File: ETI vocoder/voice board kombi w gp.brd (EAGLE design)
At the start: 160 x 60.3 mm, 170 parts, among them IC1 TL072P, IC1. TL072P, IC2 TL072P, IC2. TL072P, IC3 TL081P, IC3. TL081P, IC4 TL081P, IC4. TL081P, IC5 TL072P, IC6 LM13600AN, IC7 TL072P, IC7. TL072P, P1. C-OR-R050_075-030X100, P10. C-OR-R050_075-030X100, P13. C-OR-R050_075-030X100, P14. C-OR-R050_075-030X100, P16 C-OR-R050_075-030X100, P2. C-OR-R050_075-030X100, P5. C-OR-R050_075-030X100, P6. C-OR-R050_075-030X100, P8 C-OR-R050_075-030X100, P9. C-OR-R050_075-030X100, Q1 BF244C, Q1. BF244C, Q2 BC212L, Q2. BC212L

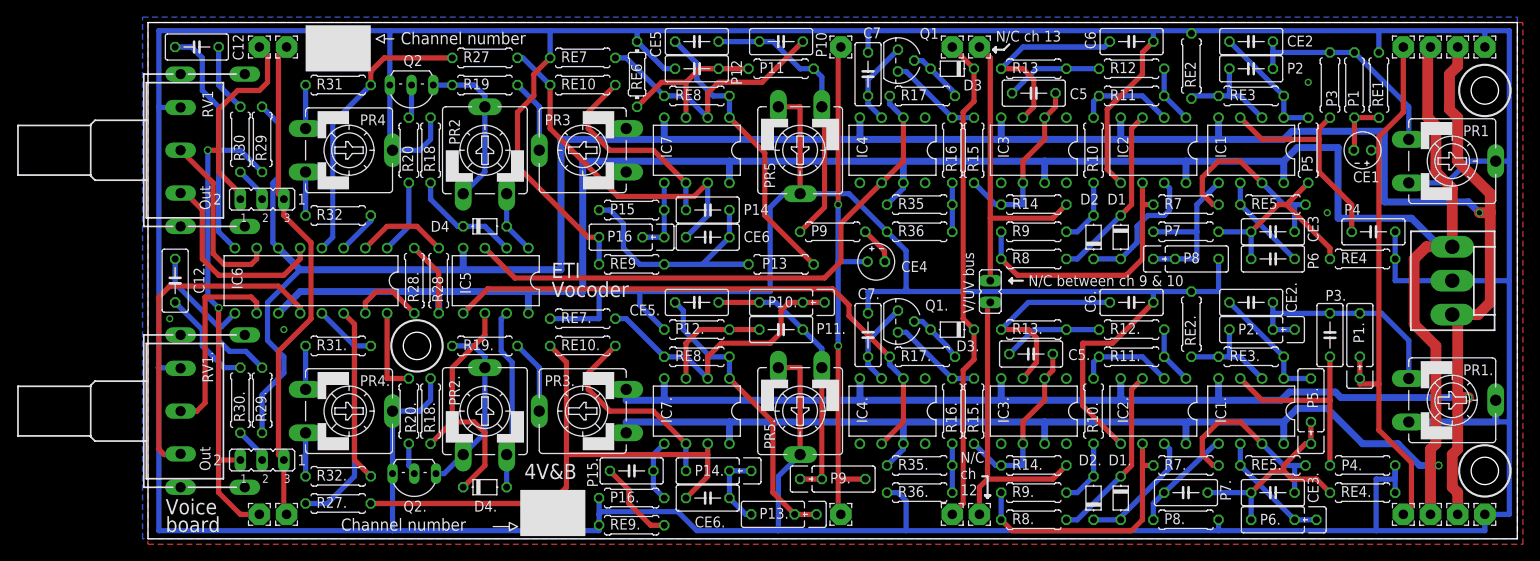
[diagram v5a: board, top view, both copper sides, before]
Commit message: Reduced board width to 2.355 inch (59.82 mm), this gives a spacing between boards of 1.1 mm, allowing a slight inaccuracy when mounting the cards next to each other
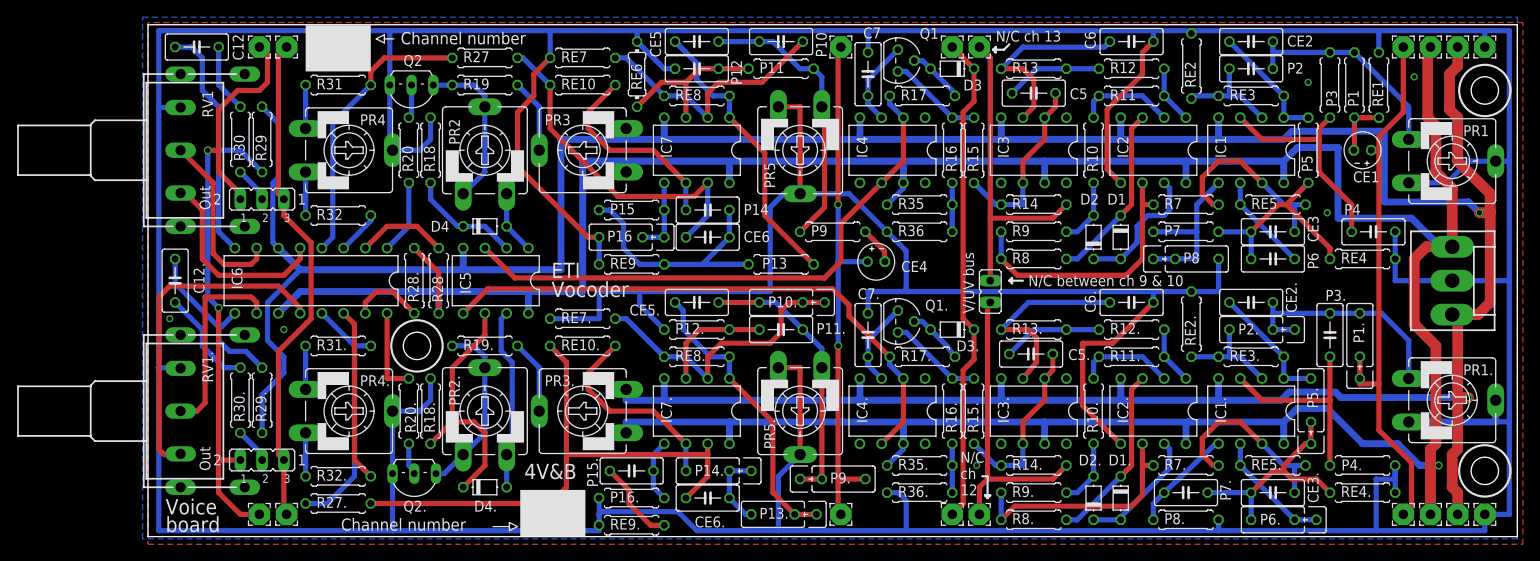
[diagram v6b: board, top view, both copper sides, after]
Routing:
- net N$54: track 30.9 -> 28.2 mm
- net GND: vias 4 -> 6
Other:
- board size 160 x 60.3 mm -> 160 x 59.8 mm
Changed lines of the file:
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@@
 <setting verticaltext="up"/>
 </settings>
-<grid distance="0.0125" unitdist="inch" unit="inch" style="dots" multiple="1" display="yes" altdistance="0.025" altunitdist="inch" altunit="inch"/>
+<grid distance="0.0125" unitdist="inch" unit="mil" style="dots" multiple="1" display="yes" altdistance="0.025" altunitdist="inch" altunit="inch"/>
 <layers>
 <layer number="1" name="Top" color="4" fill="1" visible="yes" active="yes"/>
@@
 <board>
 <plain>
-<wire x1="0" y1="0" x2="160" y2="0" width="0" layer="20"/>
-<wire x1="160" y1="0" x2="160" y2="60.325" width="0" layer="20"/>
-<wire x1="160" y1="60.325" x2="0" y2="60.325" width="0" layer="20"/>
-<wire x1="0" y1="60.325" x2="0" y2="0" width="0" layer="20"/>
+<wire x1="0" y1="0.254" x2="160" y2="0.254" width="0" layer="20"/>
+<wire x1="160" y1="0.254" x2="160" y2="60.071" width="0" layer="20"/>
+<wire x1="160" y1="60.071" x2="0" y2="60.071" width="0" layer="20"/>
+<wire x1="0" y1="60.071" x2="0" y2="0.254" width="0" layer="20"/>
 <hole x="156.21" y="52.3875" drill="3.2"/>
 <circle x="156.21" y="52.3875" radius="3" width="0.254" layer="25"/>
@@
 <wire x1="52.705" y1="1.905" x2="53.0225" y2="1.5875" width="0.6096" layer="16"/>
 <wire x1="53.0225" y1="1.5875" x2="52.705" y2="1.5875" width="0.6096" layer="16"/>
+<via x="147.955" y="53.975" extent="1-16" drill="0.5"/>
+<via x="96.8375" y="8.5725" extent="1-16" drill="0.5"/>
 </signal>
 <signal name="N$5">
@@
 <wire x1="99.695" y1="5.3975" x2="99.695" y2="2.2225" width="0.6096" layer="16"/>
 <wire x1="116.205" y1="11.1125" x2="116.205" y2="8.5725" width="0.6096" layer="1"/>
-<wire x1="116.205" y1="8.5725" x2="116.205" y2="2.2225" width="0.6096" layer="1"/>
-<wire x1="116.205" y1="2.2225" x2="114.935" y2="0.9525" width="0.6096" layer="1"/>
-<wire x1="114.935" y1="0.9525" x2="100.965" y2="0.9525" width="0.6096" layer="1"/>
-<wire x1="100.965" y1="0.9525" x2="99.695" y2="2.2225" width="0.6096" layer="1"/>
+<wire x1="116.205" y1="8.5725" x2="116.205" y2="5.08" width="0.6096" layer="1"/>
+<wire x1="116.205" y1="5.08" x2="114.935" y2="3.81" width="0.6096" layer="1"/>
+<wire x1="114.935" y1="3.81" x2="101.2825" y2="3.81" width="0.6096" layer="1"/>
+<wire x1="101.2825" y1="3.81" x2="99.695" y2="2.2225" width="0.6096" layer="1"/>
 <wire x1="117.475" y1="8.5725" x2="116.205" y2="8.5725" width="0.6096" layer="1"/>
 </signal>

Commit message: Updated trimpot names and positions
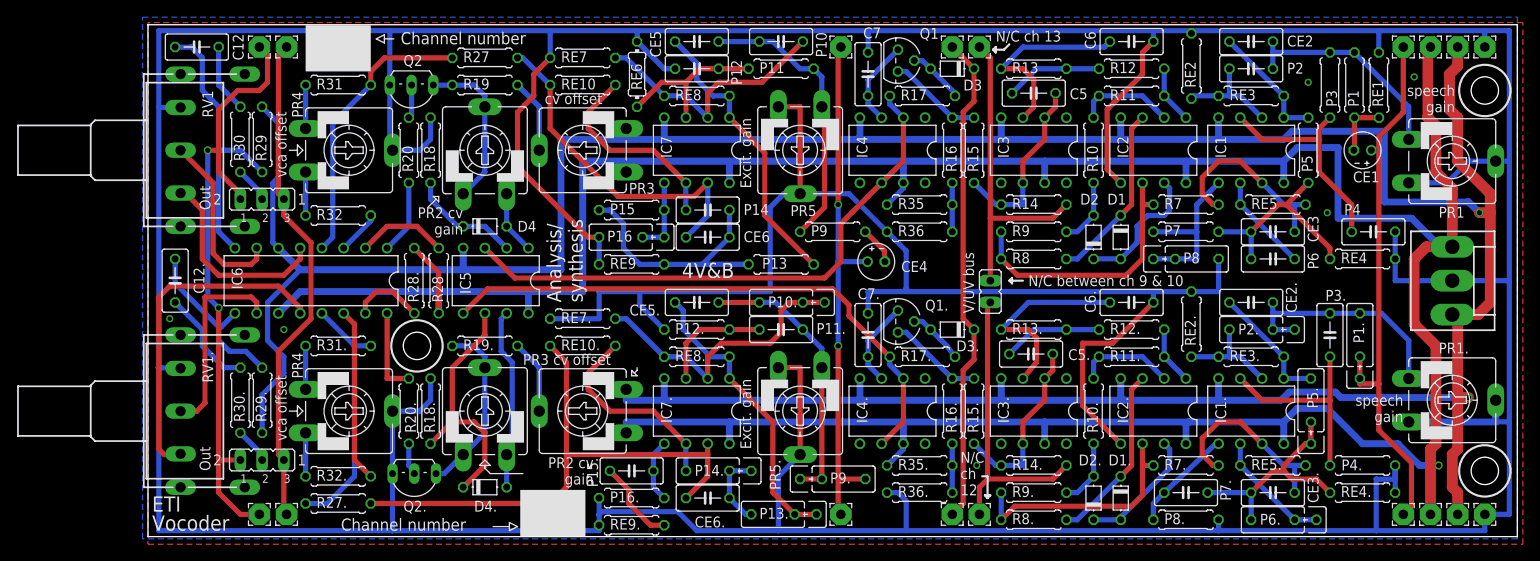
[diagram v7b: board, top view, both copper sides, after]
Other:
- board text added: "Analysis/ synthesis"
- board text added: "Excit. gain"
- board text added: "PR2 cv gain"
- board text added: "PR3"
- board text added: "PR3 cv offset"
- board text added: "PR4"
- board text added: "cv offset"
- board text added: "speech gain"
- board text added: "vca offset"
- board text removed: "Voice"
- board text removed: "board"
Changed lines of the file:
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@@
 <grid distance="0.0125" unitdist="inch" unit="mil" style="dots" multiple="1" display="yes" altdistance="0.025" altunitdist="inch" altunit="inch"/>
 <layers>
-<layer number="1" name="Top" color="4" fill="1" visible="yes" active="yes"/>
+<layer number="1" name="Top" color="4" fill="1" visible="no" active="yes"/>
 <layer number="2" name="Route2" color="1" fill="3" visible="no" active="no"/>
 <layer number="3" name="Route3" color="4" fill="3" visible="no" active="no"/>
@@
 <hole x="156.21" y="7.9375" drill="3.2"/>
 <circle x="156.21" y="7.9375" radius="3" width="0.254" layer="25"/>
-<text x="43.97375" y="6.985" size="1.778" layer="25" font="vector">4V&amp;B</text>
+<text x="62.38875" y="30.48" size="1.778" layer="25" font="vector">4V&amp;B</text>
 <text x="93.6625" y="55.5625" size="1.27" layer="26" font="vector" rot="MR270">Slew</text>
 <text x="98.425" y="55.5625" size="1.27" layer="26" font="vector" rot="MR270">V/UV</text>
@@
 <wire x1="43.18" y1="1.42875" x2="42.2275" y2="0.9525" width="0.15" layer="25"/>
 <wire x1="42.2275" y1="0.9525" x2="42.2275" y2="1.42875" width="0.15" layer="25"/>
-<text x="2.06375" y="2.8575" size="1.778" layer="25">Voice</text>
-<text x="2.06375" y="0.79375" size="1.778" layer="25">board</text>
-<text x="47.14875" y="30.48" size="1.778" layer="25">ETI</text>
-<text x="47.14875" y="28.2575" size="1.778" layer="25">Vocoder</text>
+<text x="0.47625" y="3.175" size="1.778" layer="25">ETI</text>
+<text x="0.47625" y="0.9525" size="1.778" layer="25">Vocoder</text>
 <text x="153.035" y="23.33625" size="1.27" layer="26" rot="MR270">ETI Vocoder</text>
 <text x="153.82875" y="48.10125" size="1.27" layer="26" rot="MR270">Dual voice
 board v1.0</text>
+<text x="50.8" y="27.6225" size="1.6764" layer="25" rot="R90">Analysis/
+synthesis</text>
+<text x="152.7175" y="53.0225" size="1.27" layer="25" rot="R180">speech
+gain</text>
+<text x="146.685" y="16.8275" size="1.27" layer="25" rot="R180">speech
+gain</text>
+<text x="70.485" y="10.4775" size="1.27" layer="25" rot="R90">Excit. gain</text>
+<text x="70.485" y="40.9575" size="1.27" layer="25" rot="R90">Excit. gain</text>
+<text x="46.355" y="50.8" size="1.27" layer="25">cv offset</text>
+<text x="43.815" y="20.32" size="1.27" layer="25">PR3 cv offset</text>
+<text x="52.07" y="9.525" size="1.27" layer="25" rot="R180">PR2 cv
+gain</text>
+<text x="16.1925" y="42.2275" size="1.27" layer="25" rot="R90">vca offset</text>
+<text x="16.1925" y="11.43" size="1.27" layer="25" rot="R90">vca offset</text>
+<wire x1="43.815" y1="7.62" x2="40.005" y2="7.62" width="0.127" layer="25"/>
+<wire x1="40.005" y1="7.62" x2="39.37" y2="8.255" width="0.127" layer="25"/>
+<wire x1="39.37" y1="8.255" x2="39.37" y2="8.5725" width="0.127" layer="25"/>
+<wire x1="39.37" y1="8.5725" x2="38.735" y2="8.5725" width="0.127" layer="25"/>
+<wire x1="38.735" y1="8.5725" x2="39.37" y2="9.2075" width="0.127" layer="25"/>
+<wire x1="39.37" y1="9.2075" x2="40.005" y2="8.5725" width="0.127" layer="25"/>
+<wire x1="40.005" y1="8.5725" x2="39.37" y2="8.5725" width="0.127" layer="25"/>
+<wire x1="57.15" y1="20.0025" x2="57.15" y2="19.685" width="0.127" layer="25"/>
+<wire x1="57.15" y1="19.685" x2="56.8325" y2="19.3675" width="0.127" layer="25"/>
+<wire x1="56.8325" y1="19.3675" x2="56.515" y2="19.685" width="0.127" layer="25"/>
+<wire x1="56.515" y1="19.685" x2="56.515" y2="19.05" width="0.127" layer="25"/>
+<wire x1="56.515" y1="19.05" x2="57.15" y2="19.05" width="0.127" layer="25"/>
+<wire x1="57.15" y1="19.05" x2="56.8325" y2="19.3675" width="0.127" layer="25"/>
+<text x="36.83" y="38.735" size="1.27" layer="25" rot="R180">PR2 cv
+gain</text>
+<wire x1="32.7025" y1="38.735" x2="33.655" y2="39.6875" width="0.127" layer="25"/>
+<wire x1="33.655" y1="39.6875" x2="33.3375" y2="40.005" width="0.127" layer="25"/>
+<wire x1="33.3375" y1="40.005" x2="33.9725" y2="40.005" width="0.127" layer="25"/>
+<wire x1="33.9725" y1="40.005" x2="33.9725" y2="39.37" width="0.127" layer="25"/>
+<wire x1="33.9725" y1="39.37" x2="33.655" y2="39.6875" width="0.127" layer="25"/>
+<wire x1="16.51" y1="45.4025" x2="17.4625" y2="45.4025" width="0.127" layer="25"/>
+<wire x1="17.4625" y1="45.4025" x2="17.4625" y2="46.0375" width="0.127" layer="25"/>
+<wire x1="17.4625" y1="46.0375" x2="18.0975" y2="45.4025" width="0.127" layer="25"/>
+<wire x1="18.0975" y1="45.4025" x2="17.4625" y2="44.7675" width="0.127" layer="25"/>
+<wire x1="17.4625" y1="44.7675" x2="17.4625" y2="45.4025" width="0.127" layer="25"/>
+<text x="18.0975" y="49.2125" size="1.27" layer="25" rot="R90">PR4</text>
+<text x="18.0975" y="18.7325" size="1.27" layer="25" rot="R90">PR4</text>
+<wire x1="16.51" y1="14.9225" x2="17.4625" y2="14.9225" width="0.127" layer="25"/>
+<wire x1="17.4625" y1="14.9225" x2="17.4625" y2="15.5575" width="0.127" layer="25"/>
+<wire x1="17.4625" y1="15.5575" x2="18.0975" y2="14.9225" width="0.127" layer="25"/>
+<wire x1="18.0975" y1="14.9225" x2="17.4625" y2="14.2875" width="0.127" layer="25"/>
+<wire x1="17.4625" y1="14.2875" x2="17.4625" y2="14.9225" width="0.127" layer="25"/>
+<text x="56.1975" y="40.3225" size="1.27" layer="25">PR3</text>
 </plain>
 <attributes>
@@
 </element>
 <element name="PR1" library="pot" package="CA9V" value="" x="152.4" y="44.1325" smashed="yes" rot="R270">
-<attribute name="NAME" x="153.67" y="47.0535" size="1.27" layer="25" ratio="10"/>
+<attribute name="NAME" x="150.8125" y="37.5285" size="1.27" layer="25" ratio="10"/>
 <attribute name="VALUE" x="147.32" y="37.4015" size="1.27" layer="27" ratio="10"/>
 </element>
@@
 </element>
 <element name="D4" library="diode" package="D-5" value="" x="39.37" y="36.5125" smashed="yes">
-<attribute name="NAME" x="33.02" y="35.8775" size="1.27" layer="25" ratio="10"/>
+<attribute name="NAME" x="43.18" y="35.8775" size="1.27" layer="25" ratio="10"/>
 <attribute name="VALUE" x="37.465" y="33.9725" size="1.27" layer="27" ratio="10"/>
 </element>
 <element name="PR2" library="pot" package="CA9V" value="" x="39.37" y="45.4025" smashed="yes">
-<attribute name="NAME" x="36.449" y="46.0375" size="1.27" layer="25" ratio="10" rot="R90"/>
 <attribute name="VALUE" x="46.101" y="40.3225" size="1.27" layer="27" ratio="10" rot="R90"/>
 </element>
@@
 </element>
 <element name="PR3" library="pot" package="CA9V" value="" x="50.8" y="45.4025" smashed="yes" rot="R90">
-<attribute name="NAME" x="46.355" y="48.3235" size="1.27" layer="25" ratio="10"/>
 <attribute name="VALUE" x="55.88" y="52.1335" size="1.27" layer="27" ratio="10" rot="R180"/>
 </element>
@@
 </element>
 <element name="PR4" library="pot" package="CA9V" value="" x="23.495" y="45.4025" smashed="yes" rot="R270">
-<attribute name="NAME" x="24.765" y="48.3235" size="1.27" layer="25" ratio="10"/>
 <attribute name="VALUE" x="18.415" y="38.6715" size="1.27" layer="27" ratio="10"/>
 </element>
 <element name="PR5" library="pot" package="CA9V" value="" x="76.2" y="45.4025" smashed="yes" rot="R180">
-<attribute name="NAME" x="73.279" y="40.9575" size="1.27" layer="25" ratio="10" rot="R90"/>
+<attribute name="NAME" x="78.105" y="38.989" size="1.27" layer="25" ratio="10" rot="R180"/>
 <attribute name="VALUE" x="69.469" y="50.4825" size="1.27" layer="27" ratio="10" rot="R270"/>
 </element>
@@
 </element>
 <element name="PR1." library="pot" package="CA9V" value="" x="152.4" y="16.1925" smashed="yes" rot="R270">
-<attribute name="NAME" x="153.67" y="19.1135" size="1.27" layer="25" ratio="10"/>
+<attribute name="NAME" x="150.8125" y="21.6535" size="1.27" layer="25" ratio="10"/>
 <attribute name="VALUE" x="147.32" y="9.4615" size="1.27" layer="27" ratio="10"/>
 </element>
@@
 </element>
 <element name="PR2." library="pot" package="CA9V" value="" x="39.37" y="14.9225" smashed="yes">
-<attribute name="NAME" x="36.449" y="15.5575" size="1.27" layer="25" ratio="10" rot="R90"/>
 <attribute name="VALUE" x="46.101" y="9.8425" size="1.27" layer="27" ratio="10" rot="R90"/>
 </element>
@@
 </element>
 <element name="PR3." library="pot" package="CA9V" value="" x="50.8" y="14.9225" smashed="yes" rot="R90">
-<attribute name="NAME" x="46.355" y="17.8435" size="1.27" layer="25" ratio="10"/>
 <attribute name="VALUE" x="55.88" y="21.6535" size="1.27" layer="27" ratio="10" rot="R180"/>
 </element>
@@
 </element>
 <element name="PR4." library="pot" package="CA9V" value="" x="23.495" y="14.9225" smashed="yes" rot="R270">
-<attribute name="NAME" x="24.765" y="17.8435" size="1.27" layer="25" ratio="10"/>
 <attribute name="VALUE" x="18.415" y="8.1915" size="1.27" layer="27" ratio="10"/>
 </element>
 <element name="PR5." library="pot" package="CA9V" value="" x="76.2" y="14.9225" smashed="yes" rot="R180">
-<attribute name="NAME" x="73.279" y="10.4775" size="1.27" layer="25" ratio="10" rot="R90"/>
+<attribute name="NAME" x="73.914" y="5.715" size="1.27" layer="25" ratio="10" rot="R90"/>
 <attribute name="VALUE" x="69.469" y="20.0025" size="1.27" layer="27" ratio="10" rot="R270"/>
 </element>

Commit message: Various updates while working on the real vocoder
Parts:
- moved CE4 0.32 mm to (85.1, 32.1)
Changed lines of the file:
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@@
 <grid distance="0.0125" unitdist="inch" unit="mil" style="dots" multiple="1" display="yes" altdistance="0.025" altunitdist="inch" altunit="inch"/>
 <layers>
-<layer number="1" name="Top" color="4" fill="1" visible="no" active="yes"/>
+<layer number="1" name="Top" color="4" fill="1" visible="yes" active="yes"/>
 <layer number="2" name="Route2" color="1" fill="3" visible="no" active="no"/>
 <layer number="3" name="Route3" color="4" fill="3" visible="no" active="no"/>
@@
 <attribute name="VALUE" x="143.2687" y="55.3085" size="1.27" layer="27" ratio="10" rot="R270"/>
 </element>
-<element name="CE4" library="resistor" package="E2-4" value="" x="85.09" y="32.385" smashed="yes">
-<attribute name="NAME" x="88.011" y="31.1785" size="1.27" layer="25" ratio="10"/>
-<attribute name="VALUE" x="81.661" y="29.591" size="1.27" layer="27" ratio="10"/>
+<element name="CE4" library="resistor" package="E2-4" value="" x="85.09" y="32.0675" smashed="yes">
+<attribute name="NAME" x="88.011" y="30.861" size="1.27" layer="25" ratio="10"/>
+<attribute name="VALUE" x="81.661" y="29.2735" size="1.27" layer="27" ratio="10"/>
 </element>
 <element name="P11" library="resistor" package="0207/7" value="" x="73.9775" y="54.9275" smashed="yes" rot="R180">
@@
 <wire x1="80.645" y1="57.4675" x2="80.645" y2="39.0525" width="0.6096" layer="1"/>
 <via x="80.645" y="39.0525" extent="1-16" drill="0.6"/>
-<wire x1="80.645" y1="39.0525" x2="80.645" y2="32.385" width="0.6096" layer="16"/>
+<wire x1="80.645" y1="39.0525" x2="80.645" y2="32.0675" width="0.6096" layer="16"/>
 <wire x1="80.645" y1="57.4675" x2="80.9625" y2="57.4675" width="0.6096" layer="1"/>
 <wire x1="80.9625" y1="2.8575" x2="80.645" y2="2.8575" width="0.6096" layer="1"/>
@@
 <via x="80.645" y="22.5425" extent="1-16" drill="0.6"/>
 <wire x1="80.645" y1="6.985" x2="80.645" y2="22.5425" width="0.6096" layer="1"/>
-<wire x1="80.645" y1="32.385" x2="84.074" y2="32.385" width="0.6096" layer="16"/>
-<wire x1="80.645" y1="32.385" x2="80.645" y2="22.5425" width="0.6096" layer="16"/>
+<wire x1="80.645" y1="32.0675" x2="84.074" y2="32.0675" width="0.6096" layer="16"/>
+<wire x1="80.645" y1="32.0675" x2="80.645" y2="22.5425" width="0.6096" layer="16"/>
 <contactref element="PAD3" pad="1"/>
 <contactref element="P9." pad="1"/>
@@
 <contactref element="P9" pad="1"/>
 <contactref element="CE4" pad="-"/>
-<wire x1="86.106" y1="32.385" x2="86.0425" y2="33.655" width="0.6096" layer="1"/>
+<wire x1="86.106" y1="32.0675" x2="86.0425" y2="33.655" width="0.6096" layer="1"/>
 <wire x1="86.0425" y1="33.655" x2="83.82" y2="35.8775" width="0.6096" layer="1"/>
 </signal>
@@
 <wire x1="58.7375" y1="1.5875" x2="60.325" y2="1.5875" width="0.6096" layer="1"/>
 </signal>
+<signal name="N$90">
+<via x="21.2725" y="47.9425" extent="1-16" drill="1.1"/>
+</signal>
 </signals>
